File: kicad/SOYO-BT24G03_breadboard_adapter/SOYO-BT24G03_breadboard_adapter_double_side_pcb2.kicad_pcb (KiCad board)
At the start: 2 copper layers, 26.4 x 62 mm, 4 parts, among them J1 jack, P1 CONN_01X24, P2 CONN_01X23, U1 SOYO-BT24G03

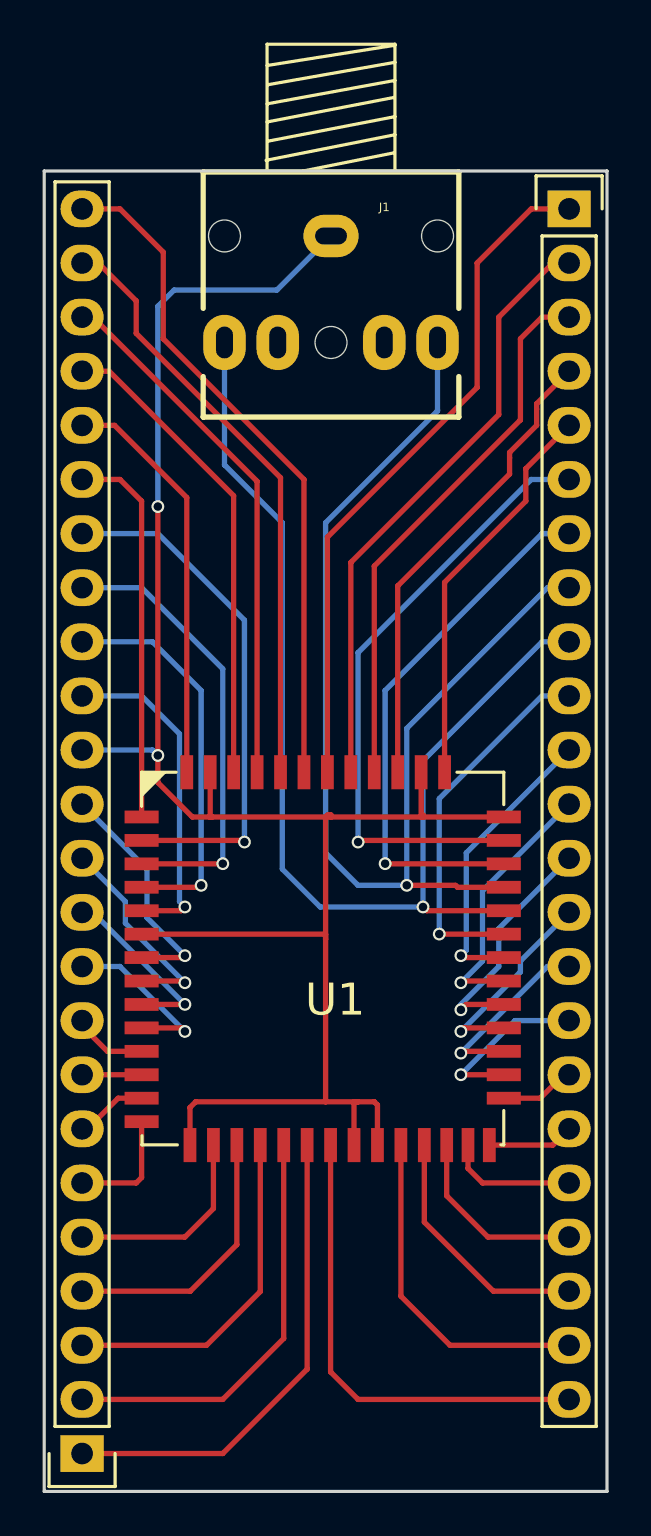
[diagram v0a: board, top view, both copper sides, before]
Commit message: AGND pin separated from GND
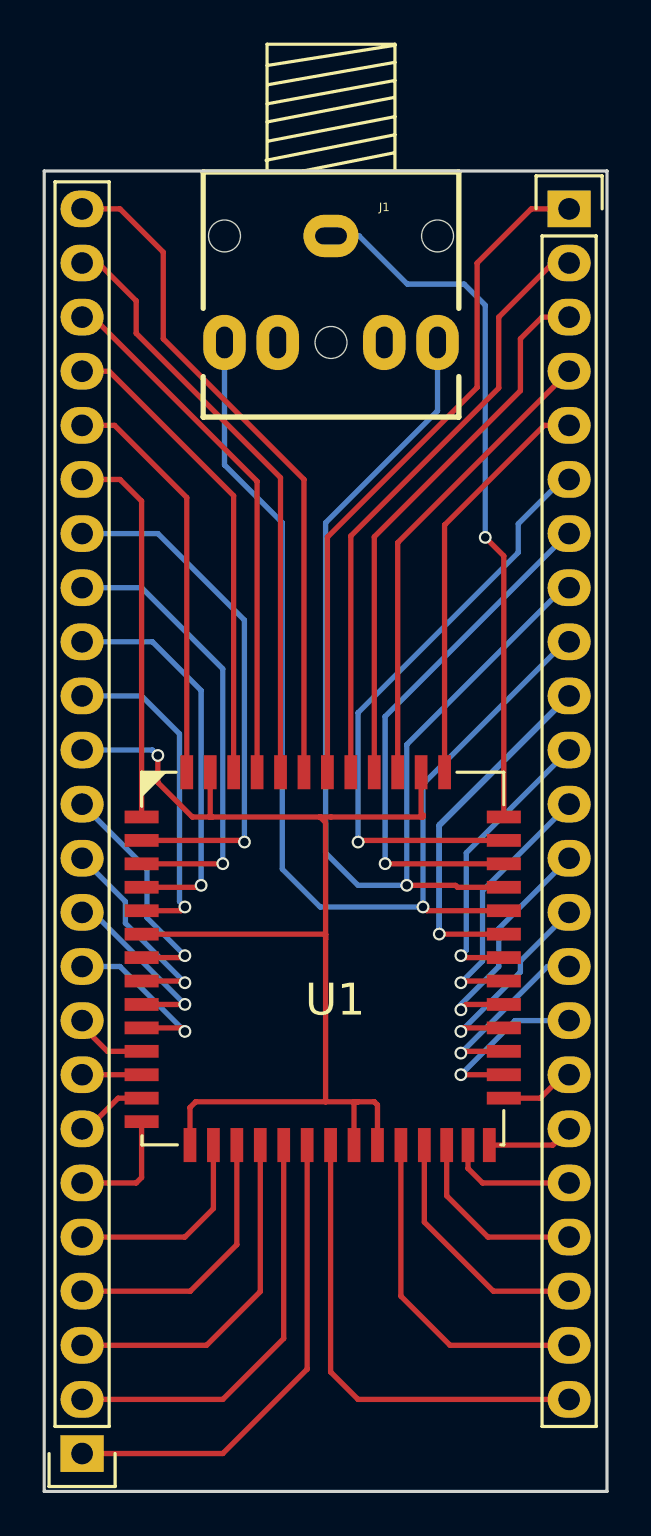
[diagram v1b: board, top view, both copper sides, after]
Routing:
- net Net-(P2-Pad10): track 17.5 -> 30.5 mm
- net Net-(P2-Pad7): track 26.9 -> 25.2 mm
- net Net-(J1-Pad1): track 94.4 -> 92.7 mm
- net Net-(P2-Pad6): track 29.0 -> 28.2 mm
- net Net-(P2-Pad5): track 19.2 -> 19.9 mm
